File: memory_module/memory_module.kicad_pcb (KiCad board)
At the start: 2 copper layers, 100 x 100 mm, 83 parts, among them SW1 SW_DIP_x08, SW2 SW_DIP_x08, SW3 SW_DIP_x08, SW4 SW_DIP_x08, SW5 SW_DIP_x08, SW6 SW_DIP_x08, SW7 SW_DIP_x08, SW8 SW_DIP_x08, U1 74HC138, U2 74HC138, U3 74LS540

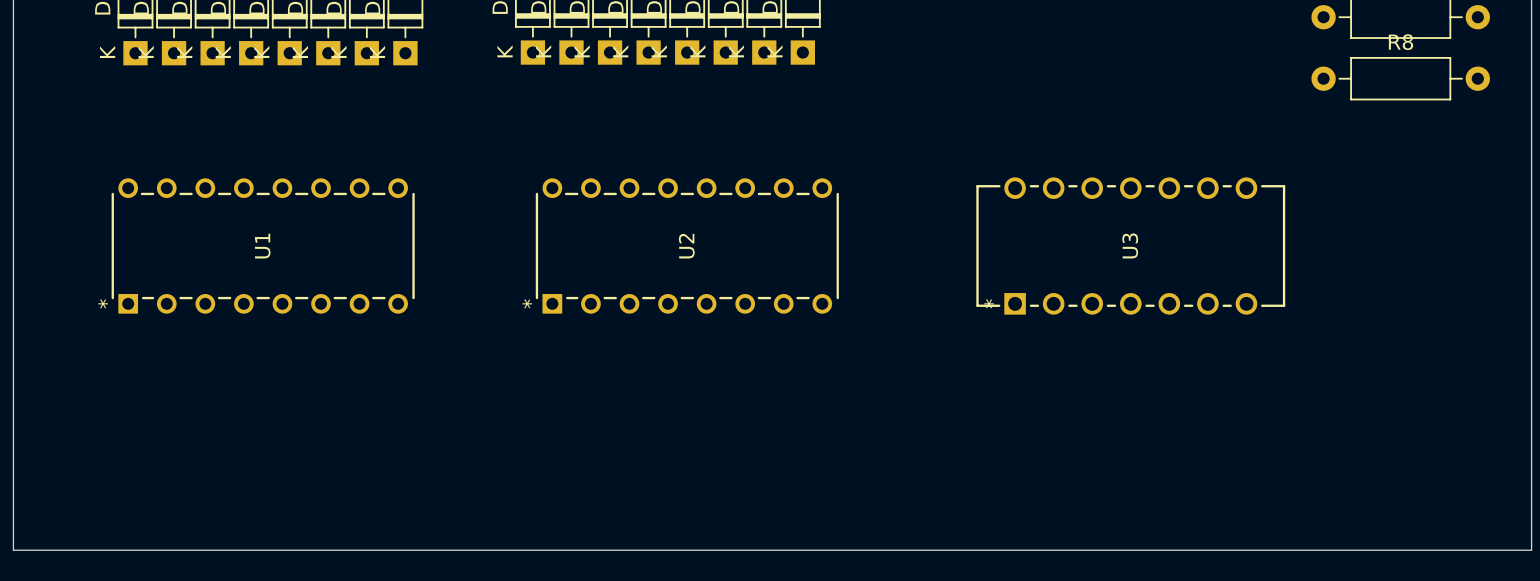
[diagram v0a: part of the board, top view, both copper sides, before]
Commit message: ICのフットプリントを追加
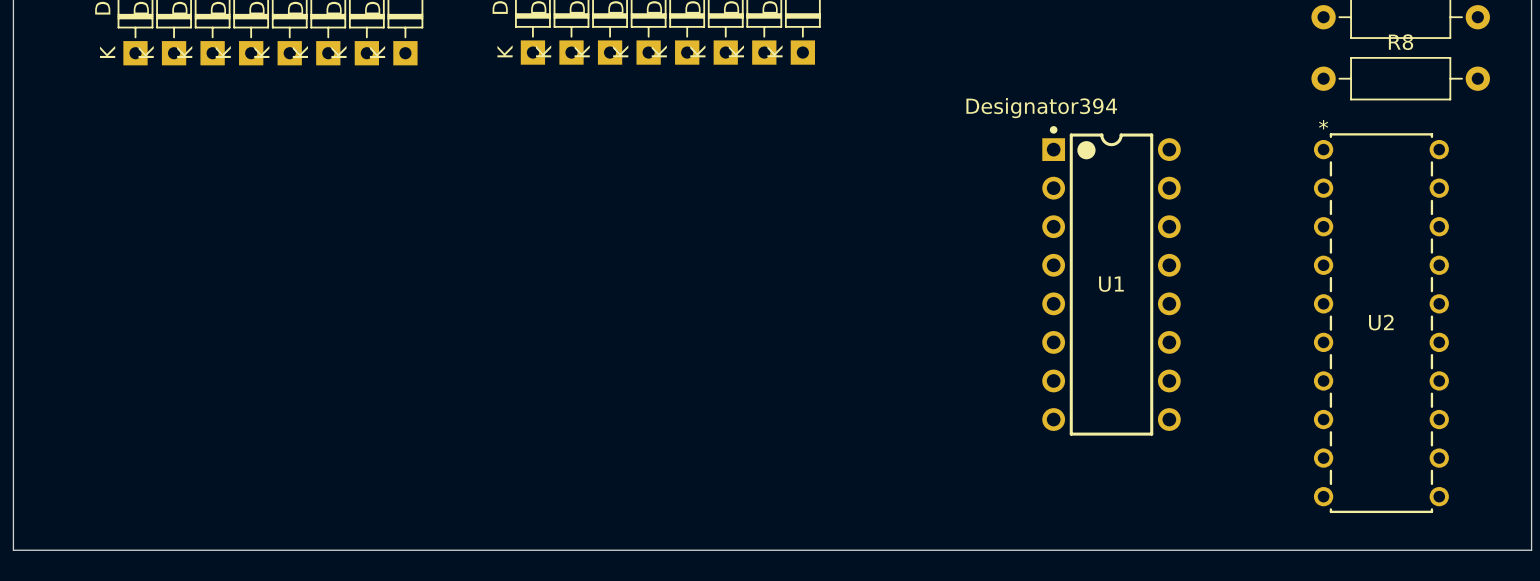
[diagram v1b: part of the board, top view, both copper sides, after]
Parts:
- removed U3: 74LS540, KiCADv6:DIP14_NTE74LS04_NTE
- U1: footprint KiCADv6:SOT38-4_NXP -> TD4_footprint:DIP16
- U2: value 74HC138 -> 74LS540; footprint KiCADv6:SOT38-4_NXP -> TD4_footprint:DIP20_TOS
- moved U1 64.8 mm to (112.4, 122.5), turned to 0 degrees
- moved U2 51.8 mm to (126.4, 113.7), turned to 0 degrees

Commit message: 回路図進めた
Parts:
- added D65: LED, LED_THT:LED_D3.0mm, F.Cu at (45.1, 57.8)
- added D66: LED, LED_THT:LED_D3.0mm, F.Cu at (75.6, 57.8)
- added D67: LED, LED_THT:LED_D3.0mm, F.Cu at (108.6, 57.8)
- added D68: LED, LED_THT:LED_D3.0mm, F.Cu at (45.1, 83.2)
- added D69: LED, LED_THT:LED_D3.0mm, F.Cu at (75.6, 83.2)
- added D70: LED, LED_THT:LED_D3.0mm, F.Cu at (108.6, 83.2)
- added D71: LED, LED_THT:LED_D3.0mm, F.Cu at (45.1, 108.6)
- added D72: LED, LED_THT:LED_D3.0mm, F.Cu at (75.6, 108.6)
- added R9: R, Resistor_THT:R_Axial_DIN0207_L6.3mm_D2.5mm_P10.16mm_Horizontal, F.Cu at (88.3, 131.4)
- moved R1 93.7 mm to (47.6, 131.4), turned to 90 degrees
- moved R2 87.2 mm to (52.7, 131.4), turned to 90 degrees
- moved R3 80.8 mm to (57.8, 131.4), turned to 90 degrees
- moved R4 74.3 mm to (62.9, 131.4), turned to 90 degrees
- moved R5 67.9 mm to (67.9, 131.4), turned to 90 degrees
- moved R6 61.5 mm to (73.0, 131.4), turned to 90 degrees
- moved R7 55.1 mm to (78.1, 131.4), turned to 90 degrees
- moved R8 48.7 mm to (83.2, 131.4), turned to 90 degrees
- moved U2 21.8 mm to (108.6, 101.0), turned to 90 degrees
- moved U1 12.7 mm to (120.0, 112.4), turned to 90 degrees
- moved D41 11.7 mm to (112.4, 87.0)
- moved D42 11.7 mm to (114.9, 87.0)
- moved D44 11.7 mm to (120.0, 87.0)
- moved D45 11.7 mm to (122.5, 87.0)
- moved D46 11.7 mm to (125.1, 87.0)
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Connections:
- D1 pad 1: unconnected-(D1-K-Pad1) -> Net-(D1-K)
- D10 pad 1: unconnected-(D10-K-Pad1) -> Net-(D10-K)
- D11 pad 1: unconnected-(D11-K-Pad1) -> Net-(D10-K)
- D12 pad 1: unconnected-(D12-K-Pad1) -> Net-(D10-K)
- D13 pad 1: unconnected-(D13-K-Pad1) -> Net-(D10-K)
- D14 pad 1: unconnected-(D14-K-Pad1) -> Net-(D10-K)
- D15 pad 1: unconnected-(D15-K-Pad1) -> Net-(D10-K)
- D16 pad 1: unconnected-(D16-K-Pad1) -> Net-(D10-K)
- D17 pad 1: unconnected-(D17-K-Pad1) -> Net-(D17-K)
- D18 pad 1: unconnected-(D18-K-Pad1) -> Net-(D17-K)
- D19 pad 1: unconnected-(D19-K-Pad1) -> Net-(D17-K)
- D2 pad 1: unconnected-(D2-K-Pad1) -> Net-(D1-K)
- D20 pad 1: unconnected-(D20-K-Pad1) -> Net-(D17-K)
- D21 pad 1: unconnected-(D21-K-Pad1) -> Net-(D17-K)
- D22 pad 1: unconnected-(D22-K-Pad1) -> Net-(D17-K)
- D23 pad 1: unconnected-(D23-K-Pad1) -> Net-(D17-K)
- D24 pad 1: unconnected-(D24-K-Pad1) -> Net-(D17-K)
- D25 pad 1: unconnected-(D25-K-Pad1) -> Net-(D25-K)
- D26 pad 1: unconnected-(D26-K-Pad1) -> Net-(D25-K)
- D27 pad 1: unconnected-(D27-K-Pad1) -> Net-(D25-K)
- D28 pad 1: unconnected-(D28-K-Pad1) -> Net-(D25-K)
- D29 pad 1: unconnected-(D29-K-Pad1) -> Net-(D25-K)
- D3 pad 1: unconnected-(D3-K-Pad1) -> Net-(D1-K)
- D30 pad 1: unconnected-(D30-K-Pad1) -> Net-(D25-K)
- D31 pad 1: unconnected-(D31-K-Pad1) -> Net-(D25-K)
- D32 pad 1: unconnected-(D32-K-Pad1) -> Net-(D25-K)
- D33 pad 1: unconnected-(D33-K-Pad1) -> Net-(D33-K)
- D34 pad 1: unconnected-(D34-K-Pad1) -> Net-(D33-K)
- D35 pad 1: unconnected-(D35-K-Pad1) -> Net-(D33-K)
- D36 pad 1: unconnected-(D36-K-Pad1) -> Net-(D33-K)
- D37 pad 1: unconnected-(D37-K-Pad1) -> Net-(D33-K)
- D38 pad 1: unconnected-(D38-K-Pad1) -> Net-(D33-K)
- D39 pad 1: unconnected-(D39-K-Pad1) -> Net-(D33-K)
- D4 pad 1: unconnected-(D4-K-Pad1) -> Net-(D1-K)
- D40 pad 1: unconnected-(D40-K-Pad1) -> Net-(D33-K)
- D41 pad 1: unconnected-(D41-K-Pad1) -> Net-(D41-K)
- D42 pad 1: unconnected-(D42-K-Pad1) -> Net-(D41-K)
- D43 pad 1: unconnected-(D43-K-Pad1) -> Net-(D41-K)
- D44 pad 1: unconnected-(D44-K-Pad1) -> Net-(D41-K)
- D45 pad 1: unconnected-(D45-K-Pad1) -> Net-(D41-K)
- D46 pad 1: unconnected-(D46-K-Pad1) -> Net-(D41-K)
- D47 pad 1: unconnected-(D47-K-Pad1) -> Net-(D41-K)
- D48 pad 1: unconnected-(D48-K-Pad1) -> Net-(D41-K)
- D49 pad 1: unconnected-(D49-K-Pad1) -> Net-(D49-K)
- D5 pad 1: unconnected-(D5-K-Pad1) -> Net-(D1-K)
- D50 pad 1: unconnected-(D50-K-Pad1) -> Net-(D49-K)
- D51 pad 1: unconnected-(D51-K-Pad1) -> Net-(D49-K)
- D52 pad 1: unconnected-(D52-K-Pad1) -> Net-(D49-K)
- D53 pad 1: unconnected-(D53-K-Pad1) -> Net-(D49-K)
- D54 pad 1: unconnected-(D54-K-Pad1) -> Net-(D49-K)
- D55 pad 1: unconnected-(D55-K-Pad1) -> Net-(D49-K)
- D56 pad 1: unconnected-(D56-K-Pad1) -> Net-(D49-K)
- D57 pad 1: unconnected-(D57-K-Pad1) -> Net-(D57-K)
- D58 pad 1: unconnected-(D58-K-Pad1) -> Net-(D57-K)
- D59 pad 1: unconnected-(D59-K-Pad1) -> Net-(D57-K)
- D6 pad 1: unconnected-(D6-K-Pad1) -> Net-(D1-K)
- D60 pad 1: unconnected-(D60-K-Pad1) -> Net-(D57-K)
- D61 pad 1: unconnected-(D61-K-Pad1) -> Net-(D57-K)
- D62 pad 1: unconnected-(D62-K-Pad1) -> Net-(D57-K)
- D63 pad 1: unconnected-(D63-K-Pad1) -> Net-(D57-K)
- D64 pad 1: unconnected-(D64-K-Pad1) -> Net-(D57-K)
- D7 pad 1: unconnected-(D7-K-Pad1) -> Net-(D1-K)
- D8 pad 1: unconnected-(D8-K-Pad1) -> Net-(D1-K)
- D9 pad 1: unconnected-(D9-K-Pad1) -> Net-(D10-K)
- R1 pad 1: unconnected-(R1-Pad1) -> Net-(U2-A7)
- R1 pad 2: unconnected-(R1-Pad2) -> +5V
- R2 pad 1: unconnected-(R2-Pad1) -> Net-(U2-A6)
- R2 pad 2: unconnected-(R2-Pad2) -> +5V
- R3 pad 1: unconnected-(R3-Pad1) -> Net-(U2-A5)
- R3 pad 2: unconnected-(R3-Pad2) -> +5V
- R4 pad 1: unconnected-(R4-Pad1) -> Net-(U2-A4)
- R4 pad 2: unconnected-(R4-Pad2) -> +5V
- R5 pad 1: unconnected-(R5-Pad1) -> Net-(U2-A3)
- R5 pad 2: unconnected-(R5-Pad2) -> +5V
- R6 pad 1: unconnected-(R6-Pad1) -> Net-(U2-A2)
- R6 pad 2: unconnected-(R6-Pad2) -> +5V
- R7 pad 1: unconnected-(R7-Pad1) -> Net-(U2-A1)
- R7 pad 2: unconnected-(R7-Pad2) -> +5V
- R8 pad 1: unconnected-(R8-Pad1) -> Net-(U2-A0)
- R8 pad 2: unconnected-(R8-Pad2) -> +5V
- SW1 pad 10: unconnected-(SW1-Pad10) -> Net-(U2-A1)
- SW1 pad 11: unconnected-(SW1-Pad11) -> Net-(U2-A2)
- SW1 pad 12: unconnected-(SW1-Pad12) -> Net-(U2-A3)
- SW1 pad 13: unconnected-(SW1-Pad13) -> Net-(U2-A4)
- SW1 pad 14: unconnected-(SW1-Pad14) -> Net-(U2-A5)
- SW1 pad 15: unconnected-(SW1-Pad15) -> Net-(U2-A6)
- SW1 pad 16: unconnected-(SW1-Pad16) -> Net-(U2-A7)
- SW1 pad 9: unconnected-(SW1-Pad9) -> Net-(U2-A0)
- SW2 pad 10: unconnected-(SW2-Pad10) -> Net-(U2-A1)
- SW2 pad 11: unconnected-(SW2-Pad11) -> Net-(U2-A2)
- SW2 pad 12: unconnected-(SW2-Pad12) -> Net-(U2-A3)
- SW2 pad 13: unconnected-(SW2-Pad13) -> Net-(U2-A4)
- SW2 pad 14: unconnected-(SW2-Pad14) -> Net-(U2-A5)
- SW2 pad 15: unconnected-(SW2-Pad15) -> Net-(U2-A6)
- SW2 pad 16: unconnected-(SW2-Pad16) -> Net-(U2-A7)
- SW2 pad 9: unconnected-(SW2-Pad9) -> Net-(U2-A0)
- SW3 pad 10: unconnected-(SW3-Pad10) -> Net-(U2-A1)
- SW3 pad 11: unconnected-(SW3-Pad11) -> Net-(U2-A2)
- SW3 pad 12: unconnected-(SW3-Pad12) -> Net-(U2-A3)
- SW3 pad 13: unconnected-(SW3-Pad13) -> Net-(U2-A4)
- SW3 pad 14: unconnected-(SW3-Pad14) -> Net-(U2-A5)
- SW3 pad 15: unconnected-(SW3-Pad15) -> Net-(U2-A6)
- SW3 pad 16: unconnected-(SW3-Pad16) -> Net-(U2-A7)
- SW3 pad 9: unconnected-(SW3-Pad9) -> Net-(U2-A0)
- SW4 pad 10: unconnected-(SW4-Pad10) -> Net-(U2-A1)
- SW4 pad 11: unconnected-(SW4-Pad11) -> Net-(U2-A2)
- SW4 pad 12: unconnected-(SW4-Pad12) -> Net-(U2-A3)
- SW4 pad 13: unconnected-(SW4-Pad13) -> Net-(U2-A4)
- SW4 pad 14: unconnected-(SW4-Pad14) -> Net-(U2-A5)
- SW4 pad 15: unconnected-(SW4-Pad15) -> Net-(U2-A6)
- SW4 pad 16: unconnected-(SW4-Pad16) -> Net-(U2-A7)
- SW4 pad 9: unconnected-(SW4-Pad9) -> Net-(U2-A0)
- SW5 pad 10: unconnected-(SW5-Pad10) -> Net-(U2-A1)
- SW5 pad 11: unconnected-(SW5-Pad11) -> Net-(U2-A2)
- SW5 pad 12: unconnected-(SW5-Pad12) -> Net-(U2-A3)
- SW5 pad 13: unconnected-(SW5-Pad13) -> Net-(U2-A4)
- SW5 pad 14: unconnected-(SW5-Pad14) -> Net-(U2-A5)
- SW5 pad 15: unconnected-(SW5-Pad15) -> Net-(U2-A6)
- SW5 pad 16: unconnected-(SW5-Pad16) -> Net-(U2-A7)
- SW5 pad 9: unconnected-(SW5-Pad9) -> Net-(U2-A0)
- SW6 pad 10: unconnected-(SW6-Pad10) -> Net-(U2-A1)
- SW6 pad 11: unconnected-(SW6-Pad11) -> Net-(U2-A2)
- SW6 pad 12: unconnected-(SW6-Pad12) -> Net-(U2-A3)
- SW6 pad 13: unconnected-(SW6-Pad13) -> Net-(U2-A4)
- SW6 pad 14: unconnected-(SW6-Pad14) -> Net-(U2-A5)
- SW6 pad 15: unconnected-(SW6-Pad15) -> Net-(U2-A6)
- SW6 pad 16: unconnected-(SW6-Pad16) -> Net-(U2-A7)
- SW6 pad 9: unconnected-(SW6-Pad9) -> Net-(U2-A0)
- SW7 pad 10: unconnected-(SW7-Pad10) -> Net-(U2-A1)
- SW7 pad 11: unconnected-(SW7-Pad11) -> Net-(U2-A2)
- SW7 pad 12: unconnected-(SW7-Pad12) -> Net-(U2-A3)
- SW7 pad 13: unconnected-(SW7-Pad13) -> Net-(U2-A4)
- SW7 pad 14: unconnected-(SW7-Pad14) -> Net-(U2-A5)
- SW7 pad 15: unconnected-(SW7-Pad15) -> Net-(U2-A6)
- SW7 pad 16: unconnected-(SW7-Pad16) -> Net-(U2-A7)
- SW7 pad 9: unconnected-(SW7-Pad9) -> Net-(U2-A0)
- SW8 pad 10: unconnected-(SW8-Pad10) -> Net-(U2-A1)
- SW8 pad 11: unconnected-(SW8-Pad11) -> Net-(U2-A2)
- SW8 pad 12: unconnected-(SW8-Pad12) -> Net-(U2-A3)
- SW8 pad 13: unconnected-(SW8-Pad13) -> Net-(U2-A4)
- SW8 pad 14: unconnected-(SW8-Pad14) -> Net-(U2-A5)
- SW8 pad 15: unconnected-(SW8-Pad15) -> Net-(U2-A6)
- SW8 pad 16: unconnected-(SW8-Pad16) -> Net-(U2-A7)
- SW8 pad 9: unconnected-(SW8-Pad9) -> Net-(U2-A0)
- U1 pad 1: unconnected-(U1-A0-Pad1) -> A0
- U1 pad 10: unconnected-(U1-~{Y5}-Pad10) -> Net-(D41-K)
- U1 pad 11: unconnected-(U1-~{Y4}-Pad11) -> Net-(D33-K)
- U1 pad 12: unconnected-(U1-~{Y3}-Pad12) -> Net-(D25-K)
- U1 pad 13: unconnected-(U1-~{Y2}-Pad13) -> Net-(D17-K)
- U1 pad 14: unconnected-(U1-~{Y1}-Pad14) -> Net-(D10-K)
- U1 pad 15: unconnected-(U1-~{Y0}-Pad15) -> Net-(D1-K)
- U1 pad 16: unconnected-(U1-VCC-Pad16) -> +5V
- U1 pad 2: unconnected-(U1-A1-Pad2) -> A1
- U1 pad 3: unconnected-(U1-A2-Pad3) -> A2
- U1 pad 4: unconnected-(U1-~{E0}-Pad4) -> +5V
- U1 pad 5: unconnected-(U1-~{E1}-Pad5) -> GND
- U1 pad 6: unconnected-(U1-E2-Pad6) -> GND
- U1 pad 7: unconnected-(U1-~{Y7}-Pad7) -> Net-(D57-K)
- U1 pad 8: unconnected-(U1-GND-Pad8) -> GND
- U1 pad 9: unconnected-(U1-~{Y6}-Pad9) -> Net-(D49-K)
- U2 pad 1: unconnected-(U2-G1-Pad1) -> GND
- U2 pad 10: unconnected-(U2-GND-Pad10) -> GND
- U2 pad 11: unconnected-(U2-Y7-Pad11) -> D7
- U2 pad 12: unconnected-(U2-Y6-Pad12) -> D6
- U2 pad 13: unconnected-(U2-Y5-Pad13) -> D5
- U2 pad 14: unconnected-(U2-Y4-Pad14) -> D4
- U2 pad 15: unconnected-(U2-Y3-Pad15) -> D3
- U2 pad 16: unconnected-(U2-Y2-Pad16) -> D2
- U2 pad 17: unconnected-(U2-Y1-Pad17) -> D1
- U2 pad 18: unconnected-(U2-Y0-Pad18) -> D0
- U2 pad 19: unconnected-(U2-G2-Pad19) -> GND
- U2 pad 2: unconnected-(U2-A0-Pad2) -> Net-(U2-A0)
- U2 pad 3: unconnected-(U2-A1-Pad3) -> Net-(U2-A1)
- U2 pad 4: unconnected-(U2-A2-Pad4) -> Net-(U2-A2)
- U2 pad 5: unconnected-(U2-A3-Pad5) -> Net-(U2-A3)
- U2 pad 6: unconnected-(U2-A4-Pad6) -> Net-(U2-A4)
- U2 pad 7: unconnected-(U2-A5-Pad7) -> Net-(U2-A5)
- U2 pad 8: unconnected-(U2-A6-Pad8) -> Net-(U2-A6)
- U2 pad 9: unconnected-(U2-A7-Pad9) -> Net-(U2-A7)

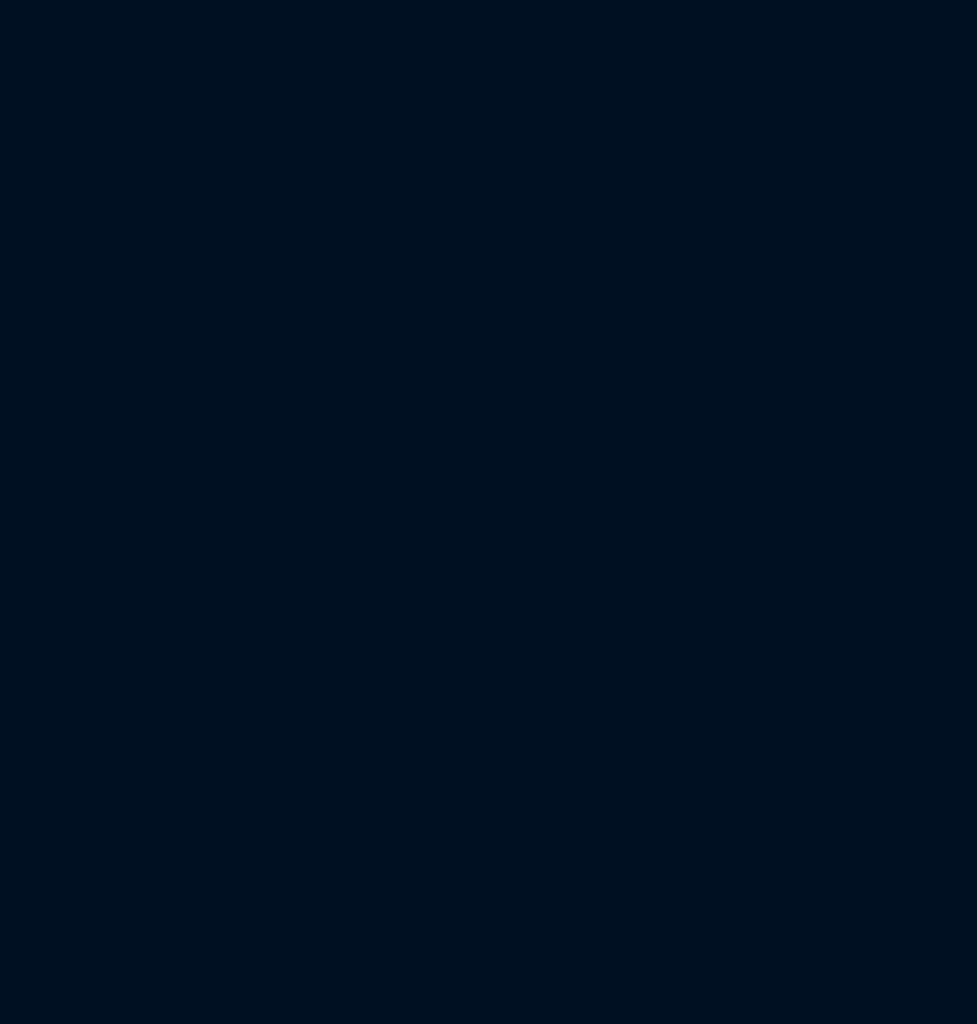
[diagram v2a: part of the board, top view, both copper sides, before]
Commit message: ピンヘッダーにフットプリントを追加
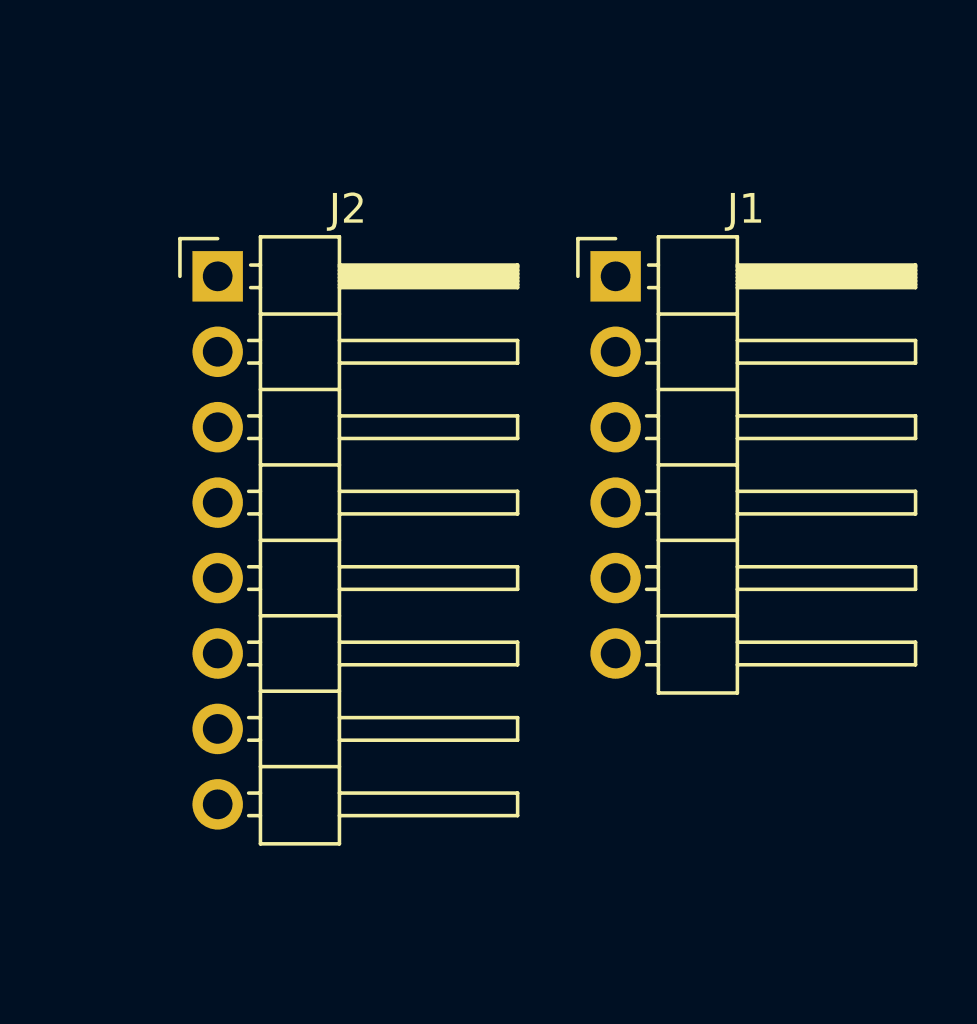
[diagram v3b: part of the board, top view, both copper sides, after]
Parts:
- added J1: Conn_01x06_Pin, Connector_PinHeader_2.54mm:PinHeader_1x06_P2.54mm_Horizontal, F.Cu at (172.1, 111.1)
- added J2: Conn_01x08_Pin, Connector_PinHeader_2.54mm:PinHeader_1x08_P2.54mm_Horizontal, F.Cu at (158.7, 111.1)
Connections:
- U2 pad 20: unconnected-(U2-VCC-Pad20) -> +5V

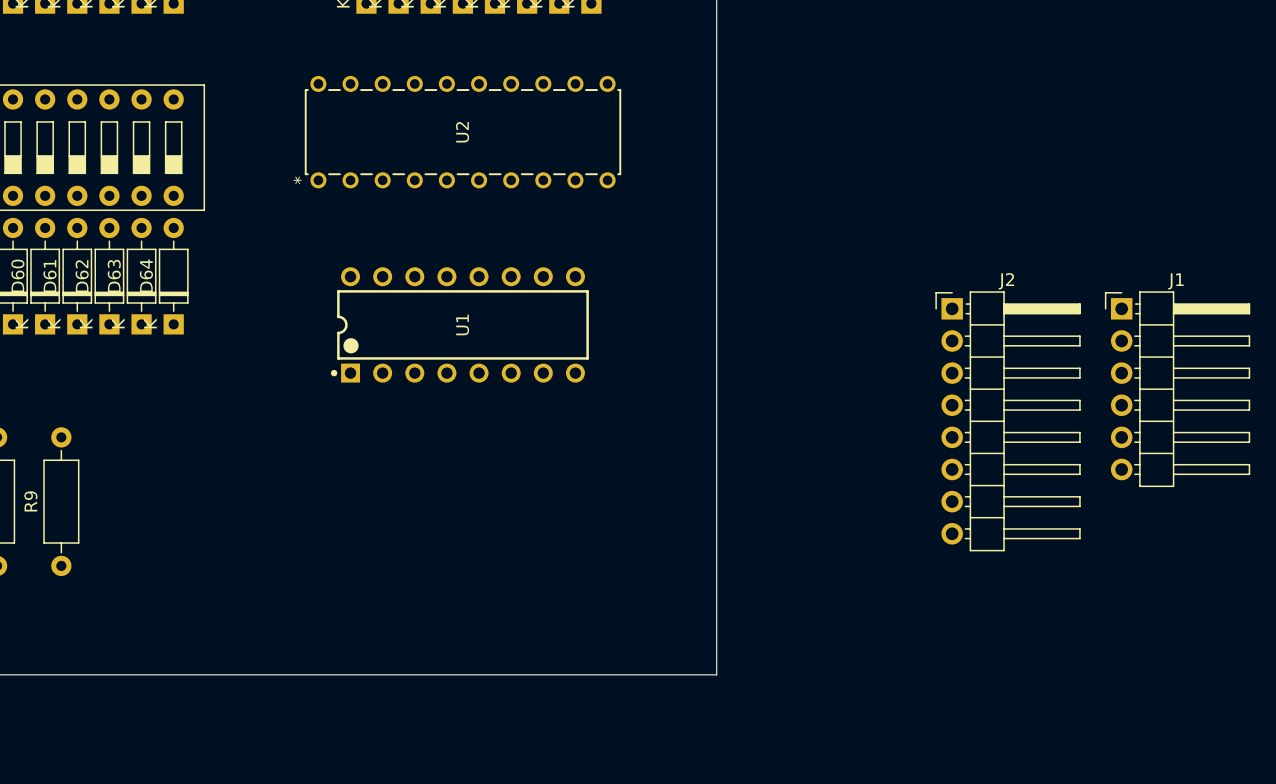
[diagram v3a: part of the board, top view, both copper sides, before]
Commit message: コネクタを配置
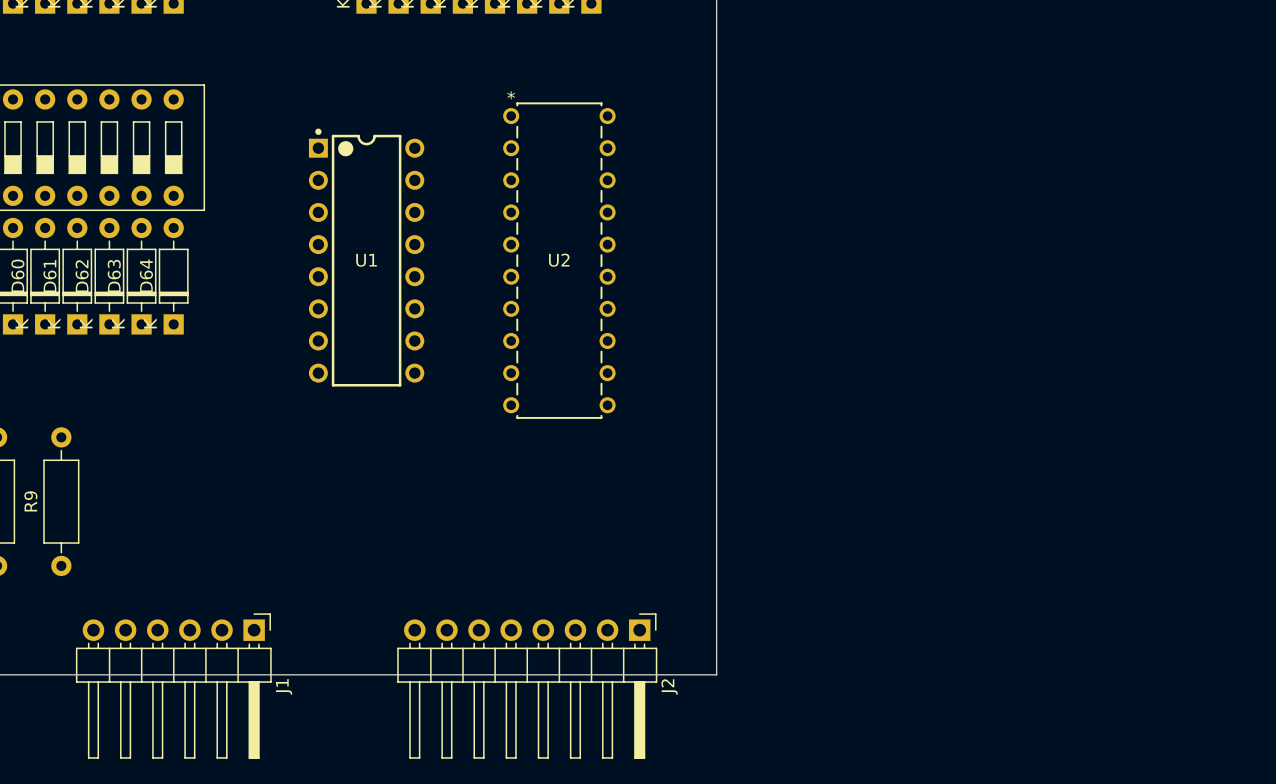
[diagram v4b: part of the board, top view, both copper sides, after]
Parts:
- U2: value 74LS540 -> 74HC540
- moved J1 73.1 mm to (103.5, 136.5), turned to -90 degrees
- moved J2 35.4 mm to (134.0, 136.5), turned to -90 degrees
- moved U2 16.1 mm to (123.8, 95.9), turned to 0 degrees
- moved U1 9.16 mm to (112.4, 107.3), turned to 0 degrees

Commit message: デザインルールを設定
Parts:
- moved U1 19.4 mm to (102.3, 123.9), turned to -90 degrees
- moved R1 12.7 mm to (47.7, 118.8), turned to -90 degrees
- moved R2 12.7 mm to (52.8, 118.8), turned to -90 degrees
- moved R3 12.7 mm to (57.8, 118.8), turned to -90 degrees
- moved R4 12.7 mm to (62.9, 118.8), turned to -90 degrees
- moved R5 12.7 mm to (68.0, 118.8), turned to -90 degrees
- moved R6 12.7 mm to (73.1, 118.8), turned to -90 degrees
- moved R7 12.7 mm to (78.2, 118.8), turned to -90 degrees
- moved R8 12.7 mm to (83.2, 118.8), turned to -90 degrees
- moved D65 6.40 mm to (45.1, 64.2)
- moved J1 5.24 mm to (108.6, 135.2)
- moved D66 5.13 mm to (75.6, 62.9)
- moved D67 5.13 mm to (108.6, 62.9)
- moved D68 5.13 mm to (45.1, 88.3)
- moved D71 5.13 mm to (45.1, 113.7)
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
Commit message: wip: 配置調整
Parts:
- moved R1 69.4 mm to (113.1, 95.5), turned to 180 degrees
- moved R2 63.0 mm to (113.1, 100.6), turned to 180 degrees
- moved R3 56.8 mm to (113.1, 105.7), turned to 180 degrees
- moved R4 50.8 mm to (113.1, 110.8), turned to 180 degrees
- moved J1 49.0 mm to (60.0, 129.0)
- moved R5 45.2 mm to (113.1, 115.8), turned to 180 degrees
- moved R6 40.1 mm to (113.1, 120.9), turned to 180 degrees
- moved R7 35.7 mm to (113.1, 126.0), turned to 180 degrees
- moved R8 32.2 mm to (113.0, 131.1), turned to 180 degrees
- moved U1 24.1 mm to (78.2, 124.8), turned to 90 degrees
- moved R9 9.07 mm to (95.1, 135.0), turned to 180 degrees
- moved J2 6.86 mm to (135.5, 129.0)
- moved D65 5.13 mm to (45.1, 59.0)
- moved D67 3.86 mm to (108.6, 59.0)
- moved D66 3.86 mm to (75.6, 59.0)
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
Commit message: フットプリント位置調整
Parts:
- moved R1 49.8 mm to (73.0, 125.1), turned to -90 degrees
- moved R2 43.7 mm to (76.8, 125.1), turned to -90 degrees
- moved U1 37.9 mm to (111.1, 106.0), turned to 0 degrees
- moved R3 37.8 mm to (80.6, 125.1), turned to -90 degrees
- moved R4 32.0 mm to (84.5, 125.1), turned to -90 degrees
- moved R5 26.5 mm to (88.3, 125.1), turned to -90 degrees
- moved R6 21.4 mm to (92.1, 125.1), turned to -90 degrees
- moved R7 17.2 mm to (95.9, 125.1), turned to -90 degrees
- moved R8 14.6 mm to (99.7, 125.1), turned to -90 degrees
- moved R9 13.0 mm to (103.5, 125.1), turned to -90 degrees
- moved D67 7.41 mm to (102.2, 62.9), turned to -90 degrees
- moved D70 7.41 mm to (102.2, 88.3), turned to -90 degrees
- moved D42 6.48 mm to (108.6, 88.3)
- moved D45 6.48 mm to (116.2, 88.3)
- moved D47 6.48 mm to (121.3, 88.3)
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
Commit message: PCBを作成
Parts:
- U1: footprint TD4_footprint:DIP16 -> TD4_footprint:DIP16_TOS
- moved R9 35.8 mm to (69.2, 135.2), turned to 90 degrees
- moved U2 24.3 mm to (136.5, 114.9), turned to -90 degrees
- moved U1 13.0 mm to (113.7, 93.3)
- moved D67 3.81 mm to (106.0, 62.9), turned to 180 degrees
- moved D70 3.81 mm to (106.0, 88.3), turned to 180 degrees
- moved D18 2.60 mm to (111.1, 62.9)
- moved D20 2.60 mm to (116.2, 62.9)
- moved D19 2.60 mm to (113.7, 62.9)
- moved D21 2.60 mm to (118.7, 62.9)
- moved D22 2.60 mm to (121.3, 62.9)
- moved D23 2.60 mm to (123.8, 62.9)
- moved D24 2.60 mm to (126.4, 62.9)
- moved D1 2.58 mm to (50.2, 62.9)
- moved D2 2.58 mm to (52.7, 62.9)
- moved D3 2.58 mm to (55.2, 62.9)
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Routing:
- net Net-(U2-A7): track 0.00 -> 337.3 mm
- net Net-(U2-A6): track 0.00 -> 304.1 mm
- net Net-(U2-A5): track 0.00 -> 298.8 mm
- net Net-(U2-A4): track 0.00 -> 293.2 mm
- net Net-(U2-A3): track 0.00 -> 288.6 mm
- net Net-(U2-A2): track 0.00 -> 285.2 mm
- net Net-(U2-A1): track 0.00 -> 282.0 mm
- net Net-(U2-A0): track 0.00 -> 278.9 mm
- net Net-(D65-A): track 0.00 -> 204.7 mm
- net GND: track 0.00 -> 154.9 mm
- net +5V: track 0.00 -> 151.2 mm
- net Net-(D1-K): track 0.00 -> 121.6 mm
- net Net-(D10-K): track 0.00 -> 95.5 mm
- net Net-(D25-K): track 0.00 -> 92.4 mm, vias 0 -> 1
- net A2: track 0.00 -> 88.2 mm
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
